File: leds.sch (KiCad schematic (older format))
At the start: 56 parts

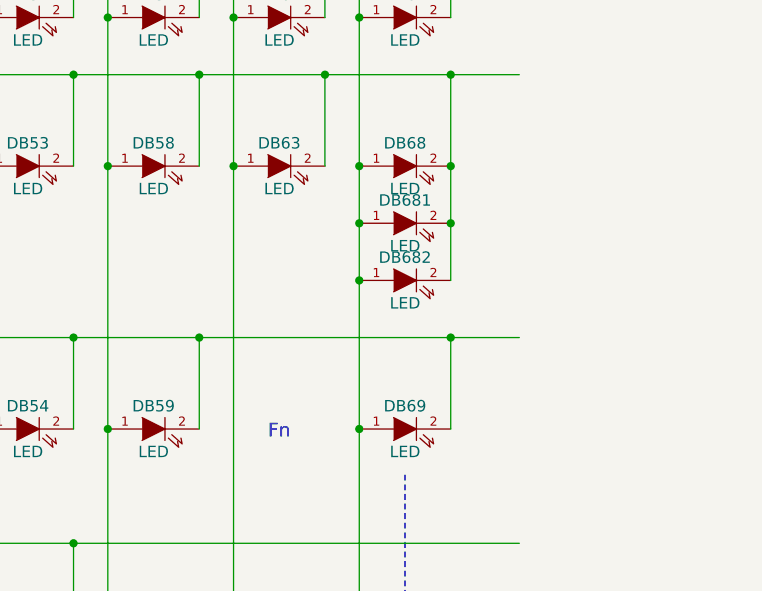
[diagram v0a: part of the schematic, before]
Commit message: Remove unnecessary SWs next to enter
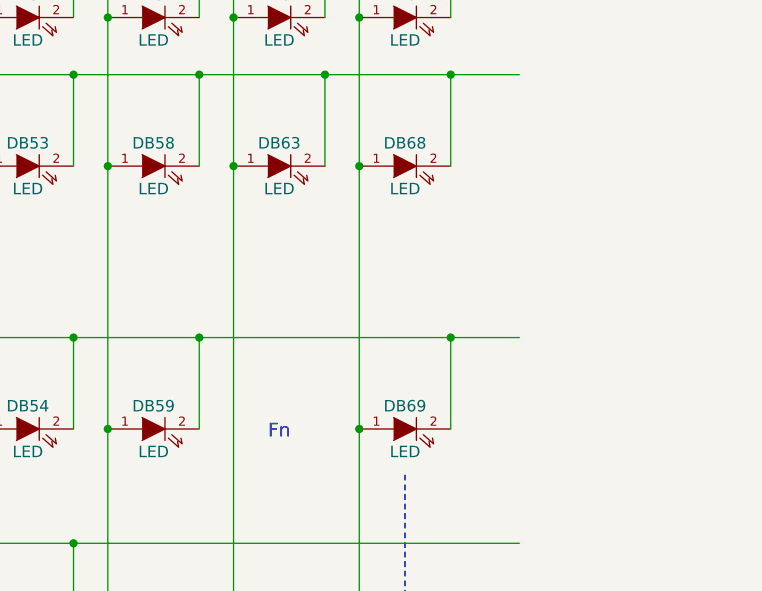
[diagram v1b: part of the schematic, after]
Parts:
- removed DB681, DB682: LED, mx1a:MX1A-led_no3d, symbol device:LED
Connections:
- wire segments 184 -> 180
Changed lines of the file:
@@
 Text Notes 8800 4700 0    60   ~ 0
 Fn
-$Comp
-L device:LED DB681
-U 1 1 51D988E8
-P 9400 3750
-F 0 "DB681" H 9400 3850 50  0000 C CNN
-F 1 "LED" H 9400 3650 50  0000 C CNN
-F 2 "mx1a:MX1A-led_no3d" H 9400 3750 60  0001 C CNN
-F 3 "" H 9400 3750 60  0001 C CNN
-	1    9400 3750
-	1    0    0    -1
-$EndComp
-$Comp
-L device:LED DB682
-U 1 1 51D988EE
-P 9400 4000
-F 0 "DB682" H 9400 4100 50  0000 C CNN
-F 1 "LED" H 9400 3900 50  0000 C CNN
-F 2 "mx1a:MX1A-led_no3d" H 9400 4000 60  0001 C CNN
-F 3 "" H 9400 4000 60  0001 C CNN
-	1    9400 4000
-	1    0    0    -1
-$EndComp
-Connection ~ 9600 3500
-Connection ~ 9600 3750
-Connection ~ 9200 3750
-Connection ~ 9200 4000
 Wire Wire Line
 	2600 1950 2600 2850
@@
 	9050 3100 9600 3100
 Wire Wire Line
-	9200 3500 9200 3750
-Wire Wire Line
 	9600 3100 9900 3100
 Wire Wire Line
@@
 	9600 4250 9900 4250
 Wire Wire Line
-	9600 3500 9600 3750
-Wire Wire Line
-	9600 3750 9600 4000
-Wire Wire Line
-	9200 3750 9200 4000
-Wire Wire Line
-	9200 4000 9200 4650
-Wire Wire Line
 	7000 4650 7000 6250
 Wire Wire Line
@@
 Wire Wire Line
 	4800 5550 4800 6250
+Wire Wire Line
+	9200 3500 9200 4650
 $EndSCHEMATC
